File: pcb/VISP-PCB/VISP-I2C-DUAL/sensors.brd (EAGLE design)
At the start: 16 x 39.9 mm, 47 parts, among them IC1 BMP388, IC2 BMP388, IC3 BMP388, IC4 BMP388, Q1 BSS138, Q2 BSS138, Q3 BSS138, Q4 BSS138, U1 MIC5225-3.3, U3 24C01ASM, U5 BMP280, U6 BMP280, U7 BMP280, U8 BMP280

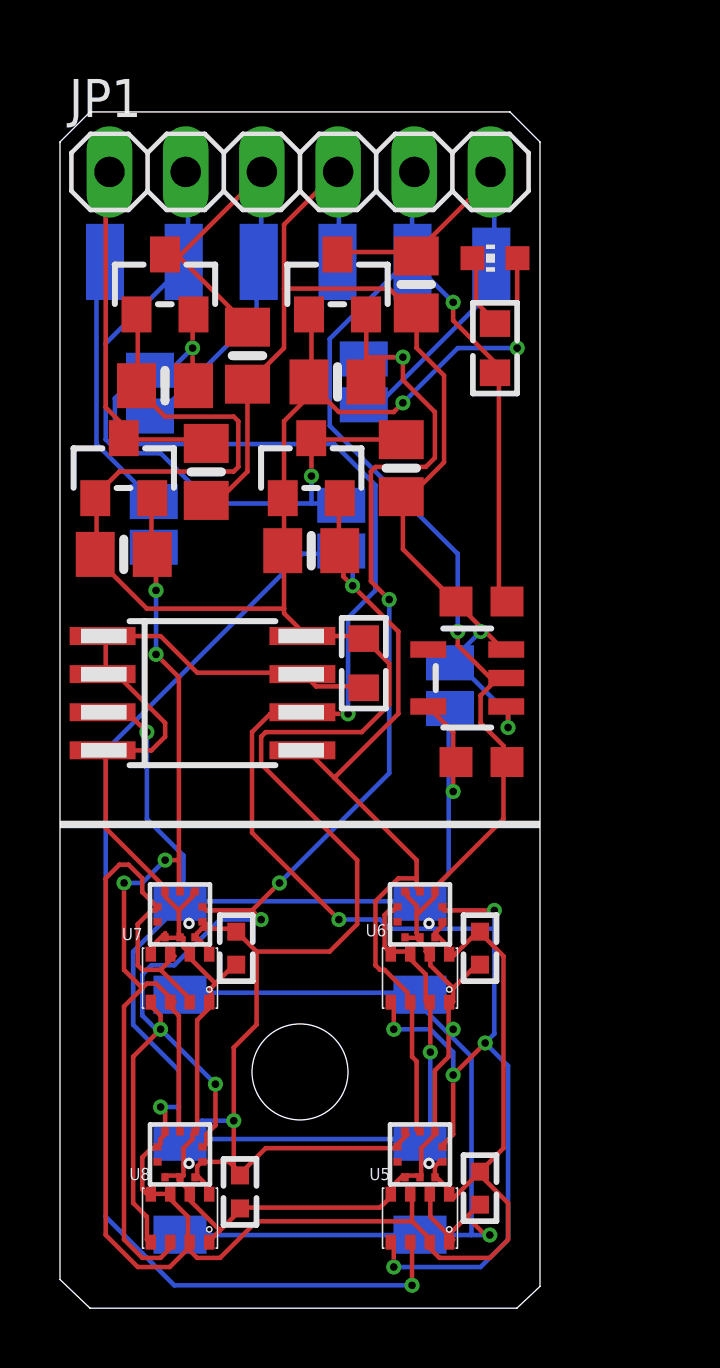
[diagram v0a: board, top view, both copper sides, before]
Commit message: JLCPCB Proven - Dual I2C board with BMP280/SLP06-007 footprints
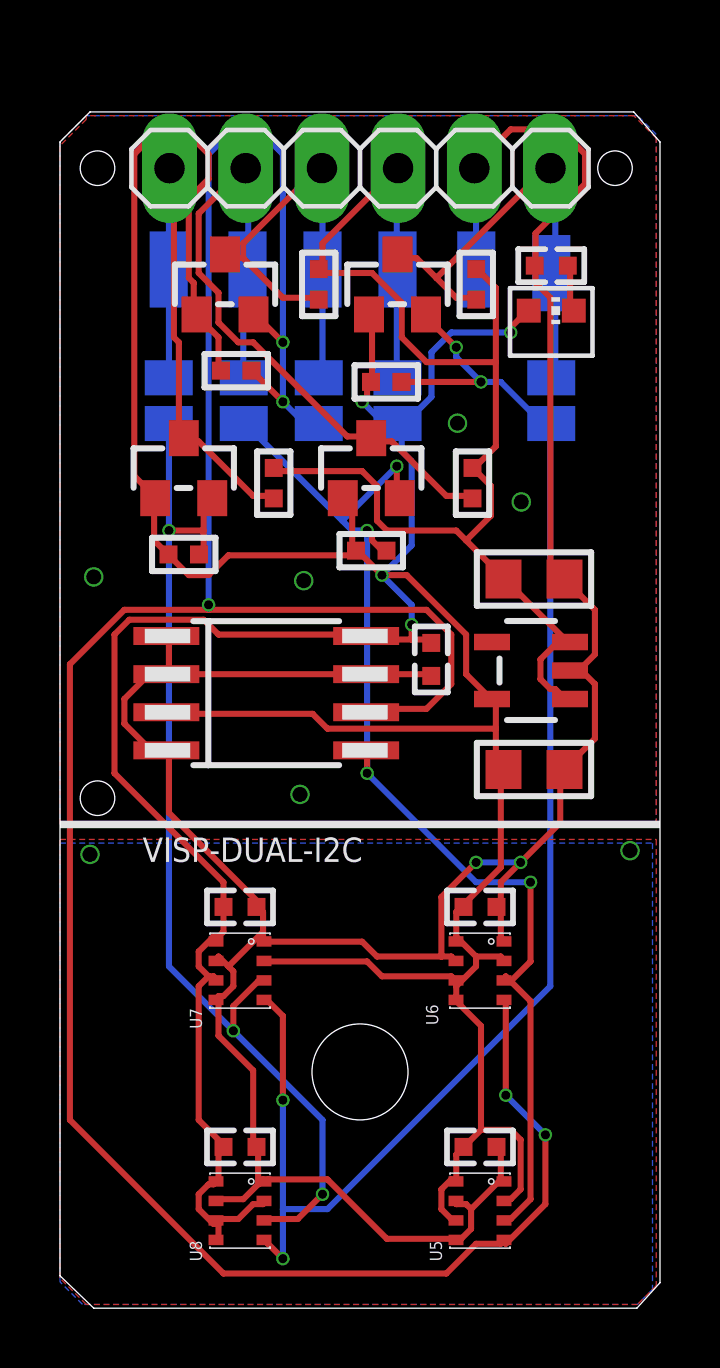
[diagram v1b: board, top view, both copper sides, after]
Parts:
- removed C10, C11, C12, C8: 100nF, Capacitor:CAP1206
- removed IC1, IC2, IC3, IC4: BMP388, microbuilder:BMP388
- added GOLD_ORB_SM1: OSHWLOGOLOGO8MM, oshw:OSHW_8MM
- C1, C3: device microbuilder:0603-NO -> microbuilder:_0805
- C9: device Capacitor:CAP0603 -> Capacitor:CAP0402
- R1, R2, R3, R5, R6, R7, R8, R9: device microbuilder:0805-NO -> microbuilder:_0402
- R4: value 47 Ohm -> 47R; device Resistor:RES0603 -> Resistor:RES0402
- moved SJ4 9.66 mm to (11.2, 30.2)
- moved SJ3 6.28 mm to (16.4, 30.2), turned to 270 degrees
- moved SJ1 5.63 mm to (8.62, 30.2), turned to 270 degrees
- moved SJ2 5.35 mm to (6.12, 30.2)
- moved SJ5 4.16 mm to (3.62, 30.2)
- moved R7 3.36 mm to (8.62, 34.1), turned to 90 degrees
- moved R4 3.33 mm to (16.4, 34.8), turned to 0 degrees
- moved LED1 2.56 mm to (16.4, 33.2), turned to 270 degrees
- moved R2 2.43 mm to (5.88, 31.2)
- moved R3 2.43 mm to (13.8, 27.5), turned to 90 degrees
- moved R9 2.28 mm to (7.12, 27.5), turned to 90 degrees
- moved C9 2.25 mm to (12.4, 21.6)
- moved GND 2.14 mm to (13.9, 34.6)
- moved SCK1 2.14 mm to (8.75, 34.6)
- moved SDA1 2.14 mm to (6.25, 34.6)
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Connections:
- net 3.3V: no longer C10.1, C11.1, C12.1, C8.1, IC1.1, IC1.10, IC1.6, IC2.1, IC2.10, IC2.5, IC2.6, IC3.1, IC3.10, IC3.6, IC4.1, IC4.10, IC4.5, IC4.6
- net GND: no longer C10.2, C11.2, C12.2, C8.2, IC1.3, IC1.5, IC1.8, IC1.9, IC2.3, IC2.8, IC2.9, IC3.3, IC3.5, IC3.8, IC3.9, IC4.3, IC4.8, IC4.9
- net SCK1_3V: no longer IC3.2, IC4.2
- net SCK2_3V: no longer IC1.2, IC2.2
- net SDI1_3V: no longer IC3.4, IC4.4
- net SDI2_3V: no longer IC1.4, IC2.4
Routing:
- net 3.3V: track 202.4 -> 141.5 mm, vias 7 -> 4
- net GND: track 135.6 -> 97.1 mm, vias 4 -> 9
- net SDI1_3V: track 67.7 -> 39.0 mm, vias 2 -> 4
- net SCK1_3V: track 66.9 -> 91.3 mm, vias 8 -> 5
- net 5.0V: track 40.3 -> 45.7 mm, vias 2 -> 0
- net SDI2_5V: track 24.0 -> 20.2 mm
- net SCK1_5V: track 18.1 -> 15.0 mm
- net SDI2_3V: track 37.6 -> 35.5 mm, vias 4 -> 3
- net SCK2_3V: track 50.3 -> 49.2 mm, vias 6 -> 4
- net LED: track 2.49 -> 1.59 mm
- net SDI1_5V: track 24.1 -> 24.2 mm, vias 1 -> 0
- added copper zone on layer 1, net GND
- added copper zone on layer 16, net GND
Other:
- board size 16 x 39.9 mm -> 20 x 39.9 mm
- board text added: "-I>I-"
- board text added: "3v Bypass: Remove Regulator"
- board text added: "Bus 1 0x54 EEPROM 0x76 BMP280 0x77 BMP280 Bus 2 (Pitots) 0x76 BMP280 0x77 BMP280"
- board text added: "[ ] BMP280 [ ] SPL06-007"
- board text removed: "-I<I-"
- board text removed: "U3 Bypass"
